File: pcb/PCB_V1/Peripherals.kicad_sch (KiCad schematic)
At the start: 32 parts, among them J301 SHT4x / XH 2.50, J302 FLOAT / 3.5 mm, J401 Molex 104031-0811, U301 PCF8563T/5, Y301 32.768k 12.5pF

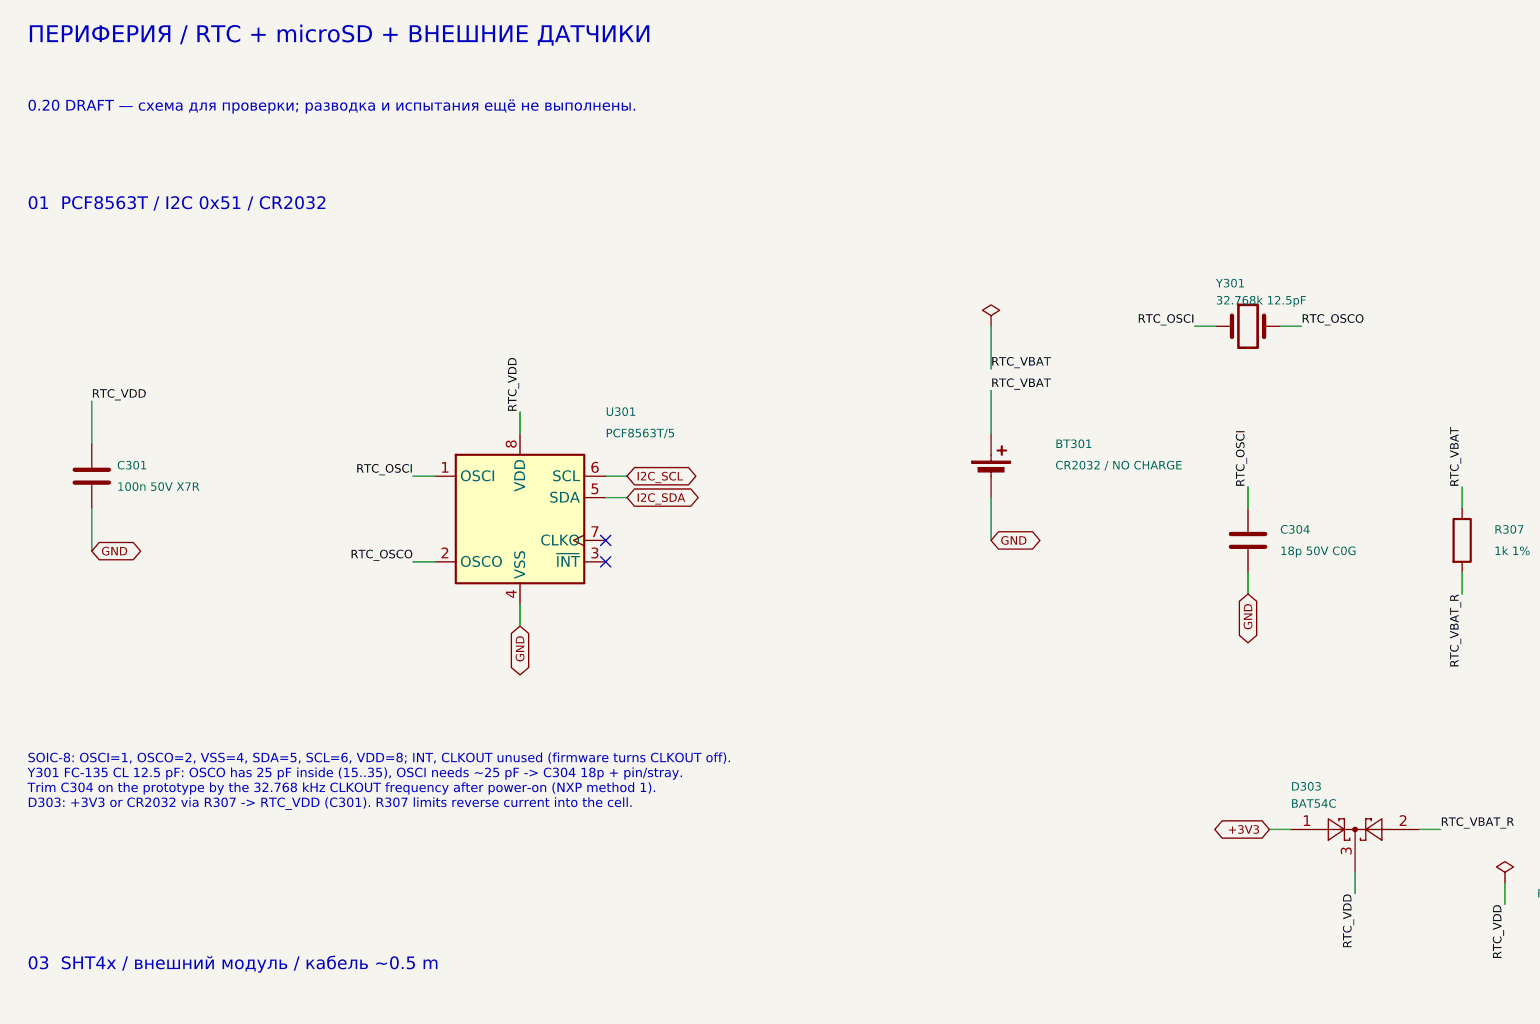
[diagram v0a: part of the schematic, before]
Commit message: pcb: use low-leakage RTC supply diode for revision 0.21
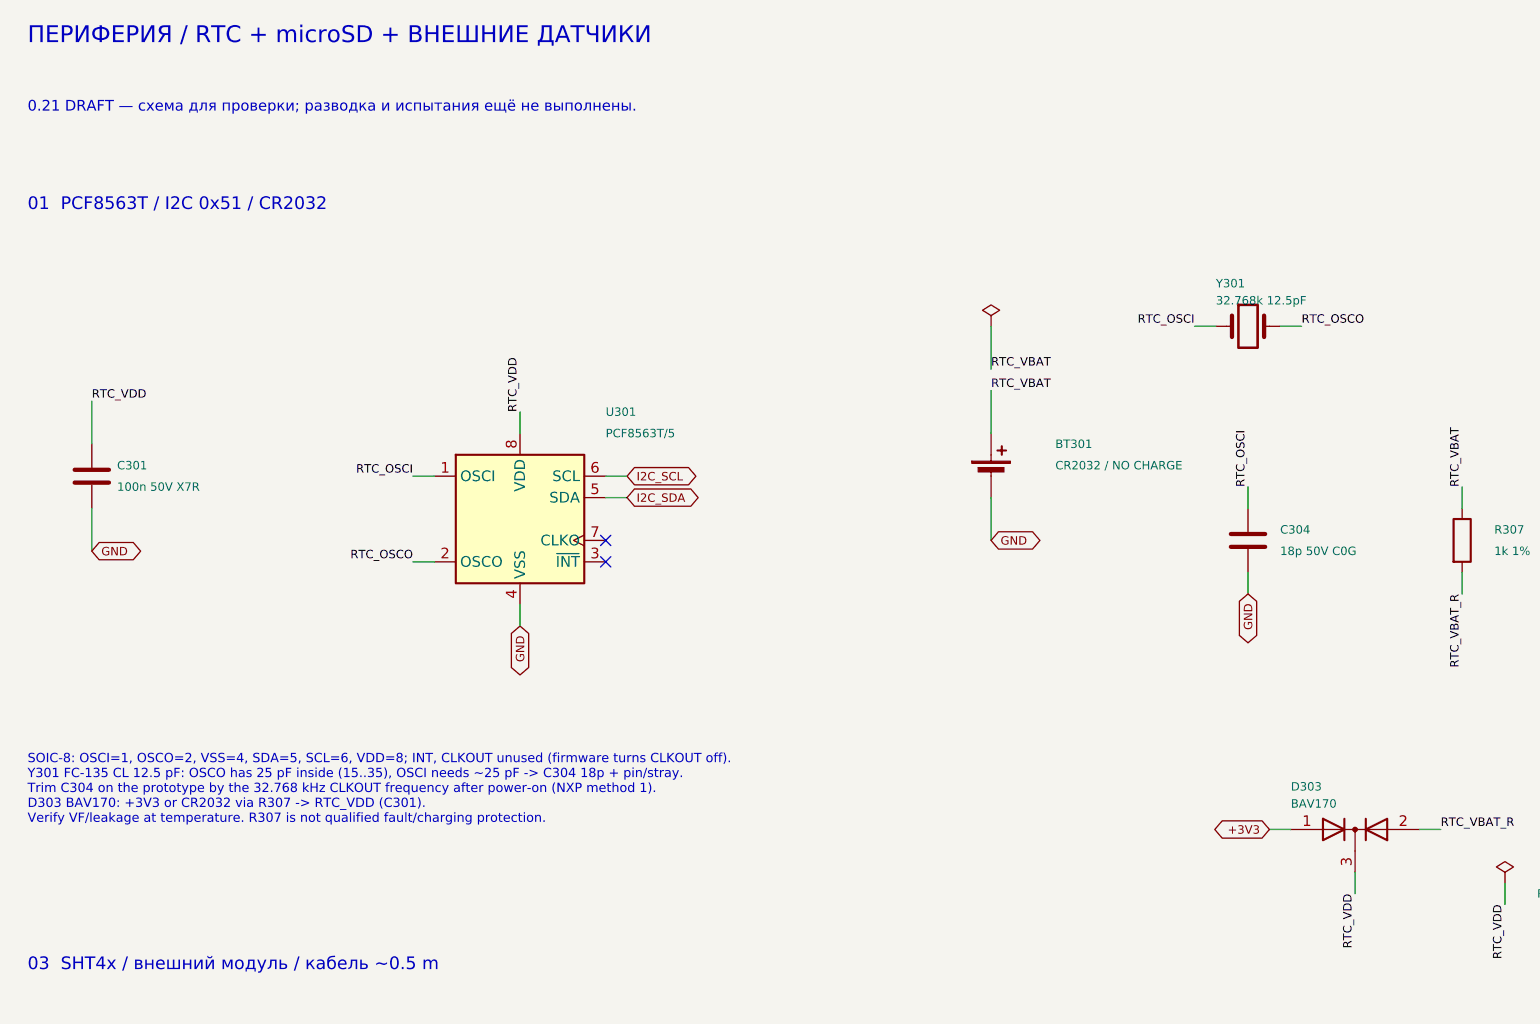
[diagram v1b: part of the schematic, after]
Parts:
- D303: value BAT54C -> BAV170; symbol Diode:BAT54C -> GrowBox:BAV170; LCSC C37704 -> C68970; MPN BAT54C,215 -> BAV170; Manufacturer Nexperia -> JSCJ
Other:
- note added: "0.21 DRAFT — схема для проверки; разводка и испытания ещё не выполнены."
- note added: "SOIC-8: OSCI=1, OSCO=2, VSS=4, SDA=5, SCL=6, VDD=8; INT, CLKOUT unused (firmware turns CLKOUT off). Y301 FC-135 CL 12.5 pF: OSCO has 25 pF inside (15..35), OSCI needs ~25 pF -> C304 18p + pin/stray. Trim C304 on the prototype by the 32.768 kHz CLKOUT frequency after power-on (NXP method 1). D303 BAV170: +3V3 or CR2032 via R307 -> RTC_VDD (C301). Verify VF/leakage at temperature. R307 is not quali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"
- note removed: "0.20 DRAFT — схема для проверки; разводка и испытания ещё не выполнены."
- note removed: "SOIC-8: OSCI=1, OSCO=2, VSS=4, SDA=5, SCL=6, VDD=8; INT, CLKOUT unused (firmware turns CLKOUT off). Y301 FC-135 CL 12.5 pF: OSCO has 25 pF inside (15..35), OSCI needs ~25 pF -> C304 18p + pin/stray. Trim C304 on the prototype by the 32.768 kHz CLKOUT frequency after power-on (NXP method 1). D303: +3V3 or CR2032 via R307 -> RTC_VDD (C301). R307 limits reverse current into the cell."
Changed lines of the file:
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@@
 	(title_block
 		(title "03 - RTC / microSD / external sensors")
-		(date "2026-09-29")
-		(rev "0.20-DRAFT")
+		(date "2026-09-30")
+		(rev "0.21-DRAFT")
 		(company "GrowBox controller")
 		(comment 1 "Simplified prototype; unrouted; hardware qualification pending")
@@
 		)
 	)
-	(text "SOIC-8: OSCI=1, OSCO=2, VSS=4, SDA=5, SCL=6, VDD=8; INT, CLKOUT unused (firmware turns CLKOUT off).\nY301 FC-135 CL 12.5 pF: OSCO has 25 pF inside (15..35), OSCI needs ~25 pF -> C304 18p + pin/stray.\nTrim C304 on the prototype by the 32.768 kHz CLKOUT frequency after power-on (NXP method 1).\nD303: +3V3 or CR2032 via R307 -> RTC_VDD (C301). R307 limits reverse current into the cell."
+	(text "SOIC-8: OSCI=1, OSCO=2, VSS=4, SDA=5, SCL=6, VDD=8; INT, CLKOUT unused (firmware turns CLKOUT off).\nY301 FC-135 CL 12.5 pF: OSCO has 25 pF inside (15..35), OSCI needs ~25 pF -> C304 18p + pin/stray.\nTrim C304 on the prototype by the 32.768 kHz CLKOUT frequency after power-on (NXP method 1).\nD303 BAV170: +3V3 or CR2032 via R307 -> RTC_VDD (C301).\nVerify VF/leakage at temperature. R307 is not qualified fault/charging protection."
 		(exclude_from_sim no)
 		(at 20.32 101.6 0)
@@
 		)
 	)
-	(text "0.20 DRAFT — схема для проверки; разводка и испытания ещё не выполнены."
+	(text "0.21 DRAFT — схема для проверки; разводка и испытания ещё не выполнены."
 		(exclude_from_sim no)
 		(at 20.32 24.13 0)
@@
 	)
 	(symbol
-		(lib_id "Diode:BAT54C")
+		(lib_id "GrowBox:BAV170")
 		(at 177.8 110.49 0)
 		(unit 1)
@@
 			)
 		)
-		(property "Value" "BAT54C"
+		(property "Value" "BAV170"
 			(at 170.18 107.44 0)
 			(effects
@@
 			)
 		)
-		(property "Datasheet" "https://www.lcsc.com/product-detail/C37704.html"
+		(property "Datasheet" "https://datasheet.lcsc.com/datasheet/pdf/6ef1dc0b67324e17a45dc6699f4d3860.pdf?productCode=C68970"
 			(at 177.8 110.49 0)
 			(effects
@@
 			)
 		)
-		(property "Manufacturer" "Nexperia"
+		(property "Manufacturer" "JSCJ"
 			(at 177.8 110.49 0)
 			(effects
@@
 			)
 		)
-		(property "MPN" "BAT54C,215"
+		(property "MPN" "BAV170"
 			(at 177.8 110.49 0)
 			(effects
@@
 			)
 		)
-		(property "LCSC" "C37704"
+		(property "LCSC" "C68970"
 			(at 177.8 110.49 0)
 			(effects
